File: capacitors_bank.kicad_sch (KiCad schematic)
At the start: 41 parts, among them K201 HF3F-L-12-1ZL2T, K202 HF3F-L-12-1ZL2T, K203 HF3F-L-12-1ZL2T, K204 HF3F-L-12-1ZL2T, K205 HF3F-L-12-1ZL2T, K206 HF3F-L-12-1ZL2T, K207 HF3F-L-12-1ZL2T, K208 HF3F-L-12-1ZL2T, Q201 PMOS, Q202 NMOS, Q203 PMOS, Q204 NMOS

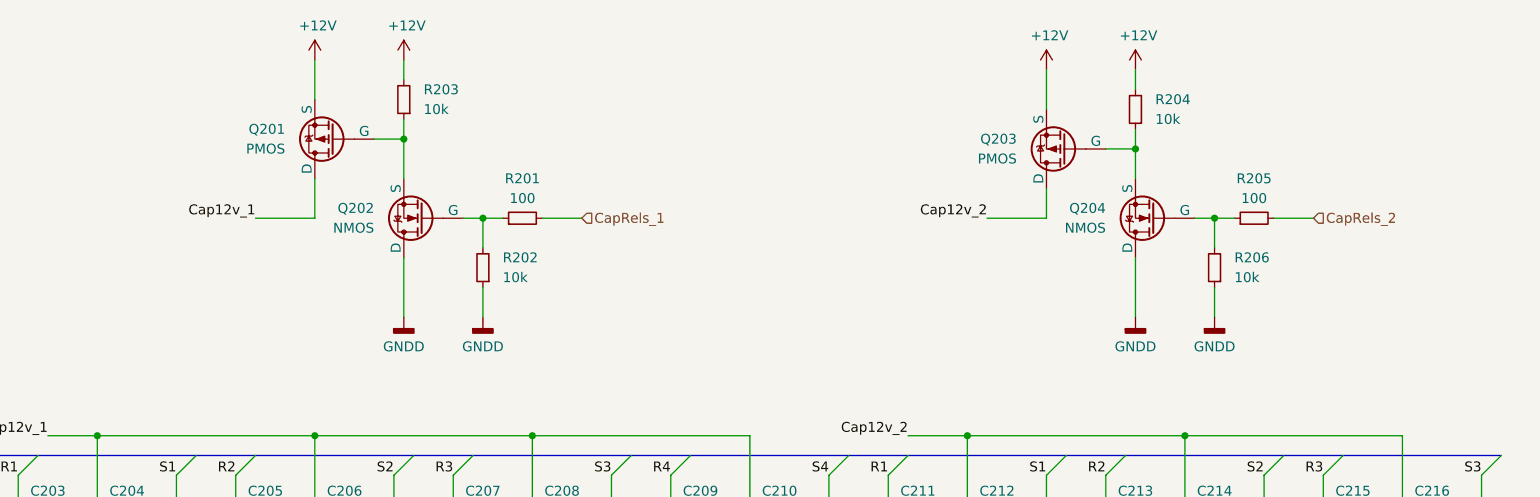
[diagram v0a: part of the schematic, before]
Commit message: Set footprints for inductors. Improved schematic of capcitors and inductors banks.
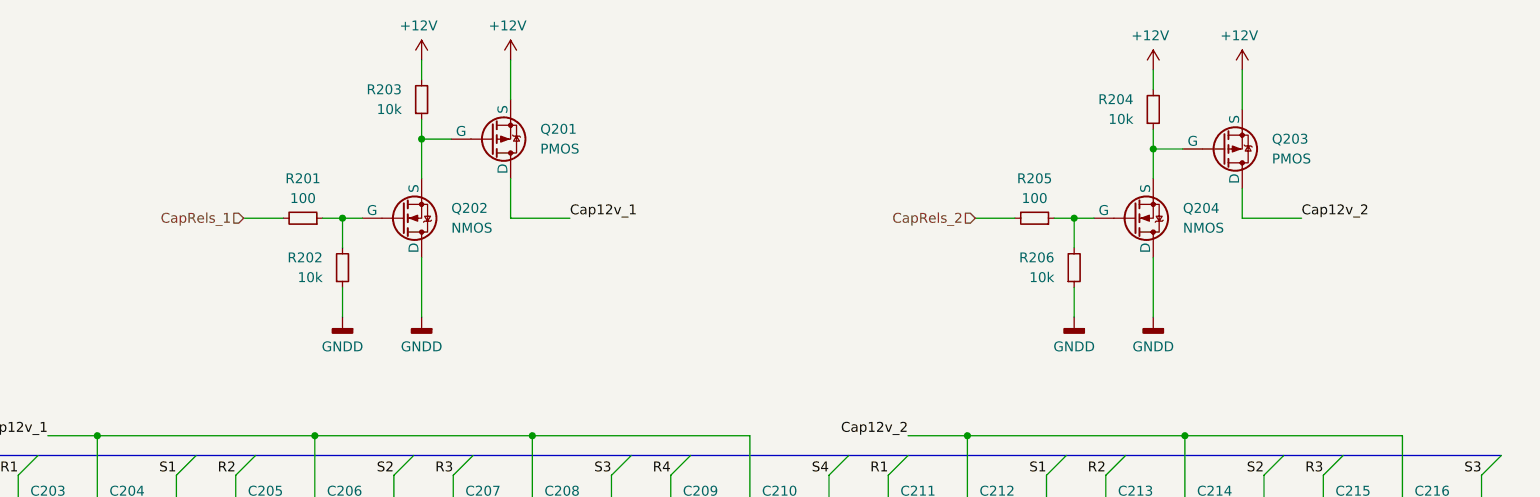
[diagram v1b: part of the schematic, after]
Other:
- moved on the sheet: Q201, Q202, Q203, Q204, R201, R202, R203, R204, R205, R206

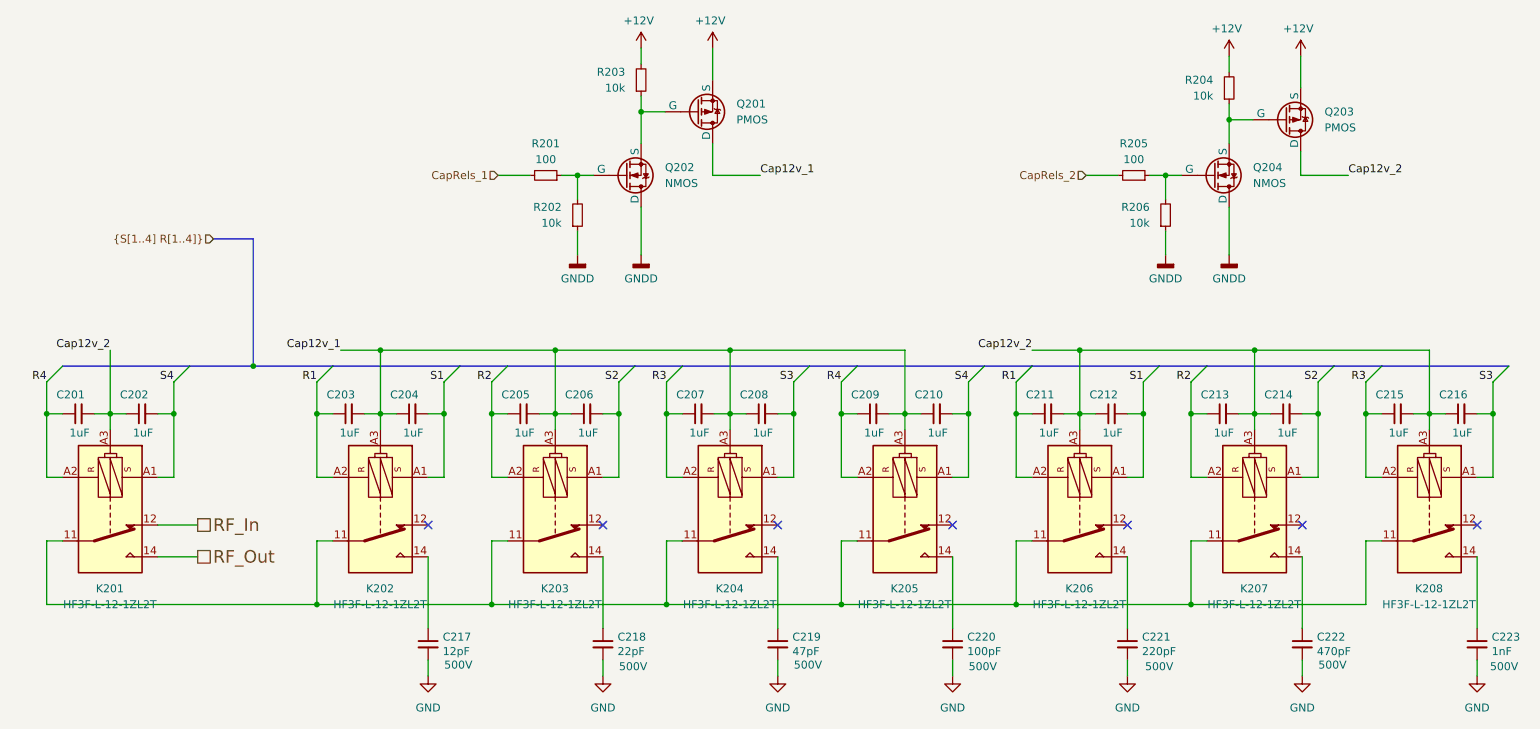
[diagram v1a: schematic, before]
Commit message: Created PDF of schematic
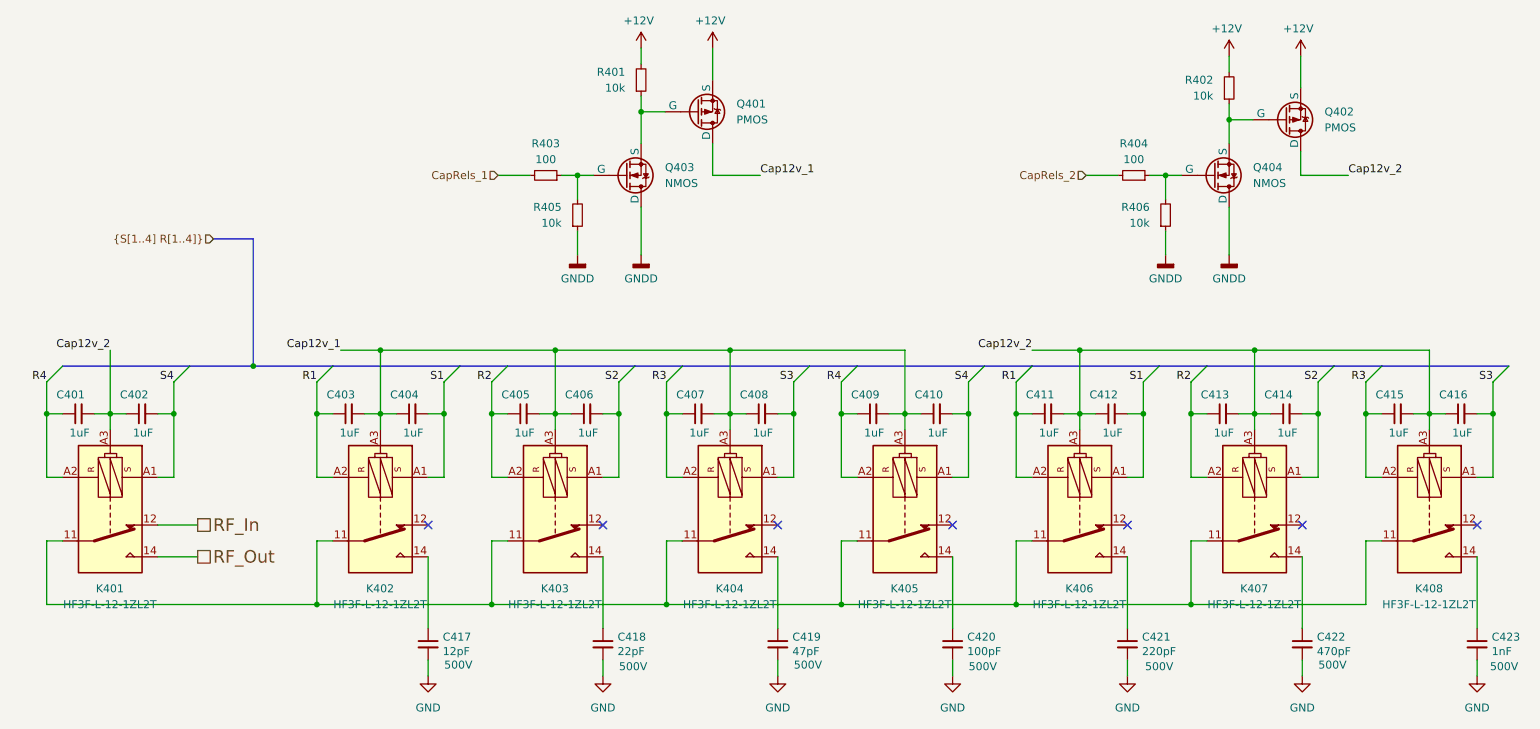
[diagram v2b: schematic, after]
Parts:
- renumbered C201 to C401, C202 to C402, C203 to C403, C204 to C404, C205 to C405, C206 to C406, C207 to C407, C208 to C408, C209 to C409, C210 to C410, C211 to C411, C212 to C412, C213 to C413, C214 to C414, C215 to C415, C216 to C416, C217 to C417, C218 to C418, C219 to C419, C220 to C420, C221 to C421, C222 to C422, C223 to C423, K201 to K401, K202 to K402, K203 to K403, K204 to K404, K205 to K405, K206 to K406, K207 to K407, K208 to K408, Q201 to Q401, Q203 to Q402, Q202 to Q403, Q204 to Q404, R203 to R401, R204 to R402, R201 to R403, R205 to R404, R202 to R405, R206 to R406

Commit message: Schematic fixes for PCB layout
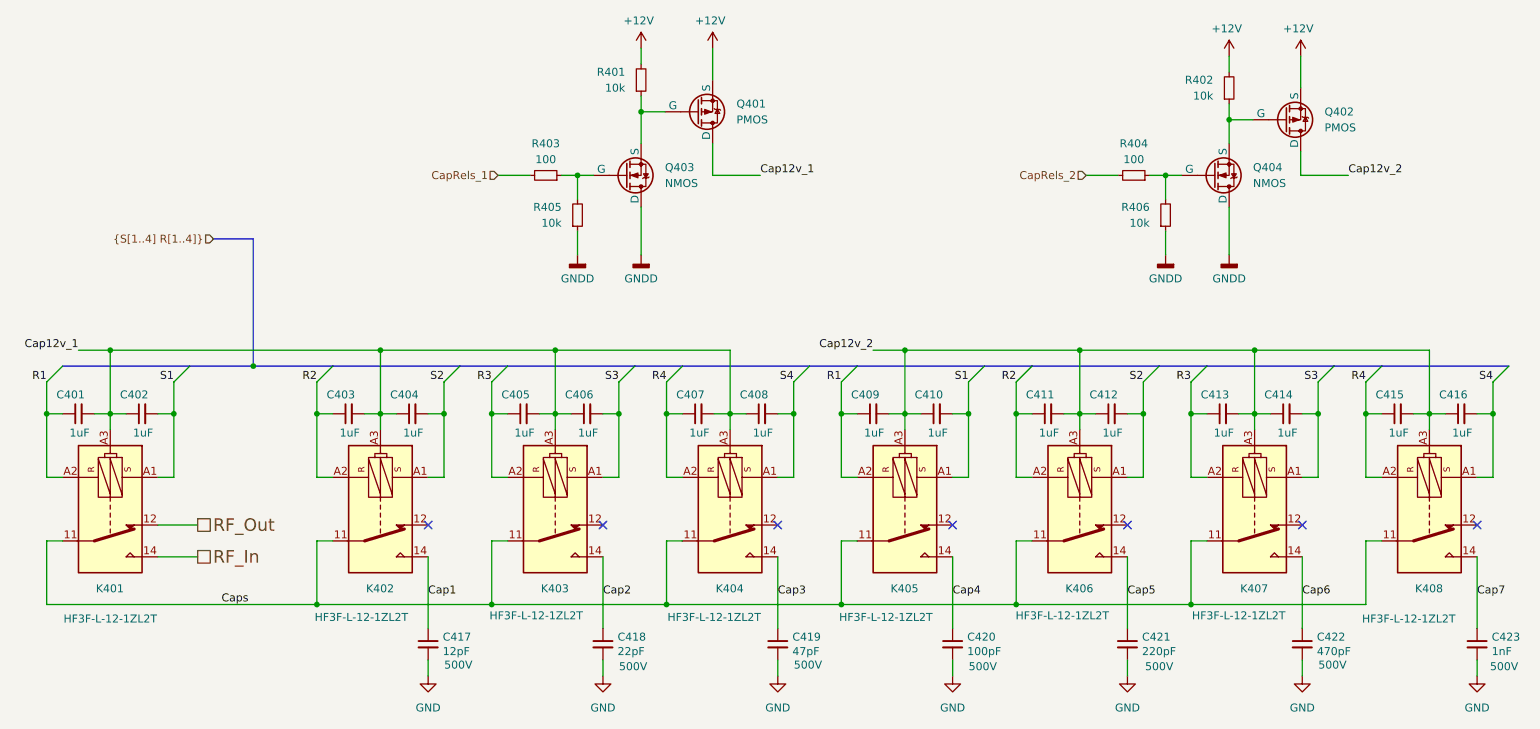
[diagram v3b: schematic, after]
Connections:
- net Cap12v_1: now also C401.2, C402.1, K401.A3; no longer C409.2, C410.1, K405.A3
- net Cap12v_2: now also C409.2, C410.1, K405.A3; no longer C401.2, C402.1, K401.A3
- net R1: now also C401.1, C409.1, K401.A2, K405.A2; no longer C403.1, C411.1, K402.A2, K406.A2
- net R2: now also C403.1, C411.1, K402.A2, K406.A2; no longer C405.1, C413.1, K403.A2, K407.A2
- net R3: now also C405.1, C413.1, K403.A2, K407.A2; no longer C407.1, C415.1, K404.A2, K408.A2
- net R4: now also C407.1, C415.1, K404.A2, K408.A2; no longer C401.1, C409.1, K401.A2, K405.A2
- net RF_In: now also K401.14; no longer K401.12
- net RF_Out: now also K401.12; no longer K401.14
- net S1: now also C402.2, C410.2, K401.A1, K405.A1; no longer C404.2, C412.2, K402.A1, K406.A1
- net S2: now also C404.2, C412.2, K402.A1, K406.A1; no longer C406.2, C414.2, K403.A1, K407.A1
- net S3: now also C406.2, C414.2, K403.A1, K407.A1; no longer C408.2, C416.2, K404.A1, K408.A1
- net S4: now also C408.2, C416.2, K404.A1, K408.A1; no longer C402.2, C410.2, K401.A1, K405.A1
- net Cap1: now reaches C417.1, K402.14
- net Caps: now reaches K401.11, K402.11, K403.11, K404.11, K405.11, K406.11, K407.11, K408.11
- net Cap2: now reaches C418.1, K403.14
- net Cap5: now reaches C421.1, K406.14
- net Cap4: now reaches C420.1, K405.14
- net Cap3: now reaches C419.1, K404.14
- net Cap6: now reaches C422.1, K407.14
- net Cap7: now reaches C423.1, K408.14
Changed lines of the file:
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@@
 	)
 	(junction
-		(at 144.78 104.14)
+		(at 127 114.3)
 		(diameter 0)
 		(color 0 0 0 0)
 	)
 	(junction
-		(at 127 114.3)
+		(at 218.44 144.78)
 		(diameter 0)
 		(color 0 0 0 0)
 	)
 	(junction
-		(at 218.44 144.78)
+		(at 172.72 114.3)
 		(diameter 0)
 		(color 0 0 0 0)
 	)
 	(junction
-		(at 172.72 114.3)
+		(at 172.72 104.14)
 		(diameter 0)
 		(color 0 0 0 0)
@@
 	)
 	(junction
+		(at 45.72 104.14)
+		(diameter 0)
+		(color 0 0 0 0)
+	)
+	(junction
 		(at 266.7 114.3)
 		(diameter 0)
@@
 	(wire
 		(pts
-			(xy 144.78 104.14) (xy 172.72 104.14)
-		)
-		(stroke
-			(width 0)
-			(type default)
-		)
-	)
-	(wire
-		(pts
 			(xy 96.52 114.3) (xy 99.06 114.3)
 		)
@@
 	(wire
 		(pts
-			(xy 82.55 104.14) (xy 88.9 104.14)
-		)
-		(stroke
-			(width 0)
-			(type default)
-		)
-	)
-	(wire
-		(pts
 			(xy 246.38 124.46) (xy 248.92 124.46)
 		)
@@
 	(wire
 		(pts
-			(xy 193.04 104.14) (xy 200.66 104.14)
-		)
-		(stroke
-			(width 0)
-			(type default)
-		)
-	)
-	(wire
-		(pts
 			(xy 127 109.22) (xy 127 114.3)
 		)
@@
 	(wire
 		(pts
+			(xy 167.64 104.14) (xy 172.72 104.14)
+		)
+		(stroke
+			(width 0)
+			(type default)
+		)
+	)
+	(wire
+		(pts
 			(xy 190.5 134.62) (xy 193.04 134.62)
 		)
@@
 	(wire
 		(pts
+			(xy 45.72 104.14) (xy 88.9 104.14)
+		)
+		(stroke
+			(width 0)
+			(type default)
+		)
+	)
+	(wire
+		(pts
 			(xy 96.52 153.67) (xy 96.52 156.21)
 		)
@@
 	(wire
 		(pts
+			(xy 40.64 104.14) (xy 45.72 104.14)
+		)
+		(stroke
+			(width 0)
+			(type default)
+		)
+	)
+	(wire
+		(pts
 			(xy 144.78 104.14) (xy 144.78 114.3)
 		)
@@
 	(wire
 		(pts
+			(xy 172.72 104.14) (xy 200.66 104.14)
+		)
+		(stroke
+			(width 0)
+			(type default)
+		)
+	)
+	(wire
+		(pts
 			(xy 224.536 81.28) (xy 224.536 88.9)
 		)
@@
 		)
 	)
+	(label "Caps"
+		(at 63.5 144.78 0)
+		(fields_autoplaced yes)
+		(effects
+			(font
+				(size 1.27 1.27)
+			)
+			(justify left bottom)
+		)
+	)
 	(label "S3"
-		(at 154.94 109.22 180)
+		(at 127 109.22 180)
 		(fields_autoplaced yes)
 		(effects
@@
 	)
 	(label "R2"
-		(at 106.68 109.22 180)
+		(at 78.74 109.22 180)
 		(fields_autoplaced yes)
 		(effects
@@
 		)
 	)
-	(label "S3"
-		(at 266.7 109.22 180)
+	(label "Cap3"
+		(at 152.4 143.51 0)
 		(fields_autoplaced yes)
 		(effects
@@
 				(size 1.27 1.27)
 			)
-			(justify right bottom)
+			(justify left bottom)
 		)
 	)
-	(label "S2"
+	(label "Cap1"
+		(at 96.52 143.51 0)
+		(fields_autoplaced yes)
+		(effects
+			(font
+				(size 1.27 1.27)
+			)
+			(justify left bottom)
+		)
+	)
+	(label "S3"
 		(at 238.76 109.22 180)
 		(fields_autoplaced yes)
@@
 		)
 	)
-	(label "S1"
+	(label "S2"
 		(at 210.82 109.22 180)
 		(fields_autoplaced yes)
@@
 		)
 	)
-	(label "S4"
+	(label "S1"
 		(at 182.88 109.22 180)
 		(fields_autoplaced yes)
@@
 		)
 	)
-	(label "S1"
-		(at 99.06 109.22 180)
+	(label "S4"
+		(at 266.7 109.22 180)
 		(fields_autoplaced yes)
 		(effects
@@
 		)
 	)
-	(label "Cap12v_2"
-		(at 193.04 104.14 180)
+	(label "S1"
+		(at 55.88 109.22 180)
 		(fields_autoplaced yes)
 		(effects
@@
 	)
 	(label "Cap12v_2"
-		(at 45.72 104.14 180)
+		(at 167.64 104.14 180)
 		(fields_autoplaced yes)
 		(effects
@@
 		)
 	)
+	(label "Cap6"
+		(at 236.22 143.51 0)
+		(fields_autoplaced yes)
+		(effects
+			(font
+				(size 1.27 1.27)
+			)
+			(justify left bottom)
+		)
+	)
+	(label "Cap4"
+		(at 180.34 143.51 0)
+		(fields_autoplaced yes)
+		(effects
+			(font
+				(size 1.27 1.27)
+			)
+			(justify left bottom)
+		)
+	)
 	(label "Cap12v_2"
 		(at 243.586 76.2 0)
@@
 	)
 	(label "Cap12v_1"
-		(at 82.55 104.14 180)
+		(at 40.64 104.14 180)
 		(fields_autoplaced yes)
 		(effects
@@
 	)
 	(label "R4"
-		(at 35.56 109.22 180)
+		(at 134.62 109.22 180)
 		(fields_autoplaced yes)
 		(effects
@@
 	)
 	(label "S2"
-		(at 127 109.22 180)
+		(at 99.06 109.22 180)
 		(fields_autoplaced yes)
 		(effects
@@
 	)
 	(label "R1"
-		(at 190.5 109.22 180)
+		(at 162.56 109.22 180)
 		(fields_autoplaced yes)
 		(effects
@@
 	)
 	(label "R3"
-		(at 134.62 109.22 180)
+		(at 106.68 109.22 180)
 		(fields_autoplaced yes)
 		(effects
@@
 		)
 	)
+	(label "Cap7"
+		(at 264.16 143.51 0)
+		(fields_autoplaced yes)
+		(effects
+			(font
+				(size 1.27 1.27)
+			)
+			(justify left bottom)
+		)
+	)
 	(label "R3"
-		(at 246.38 109.22 180)
+		(at 218.44 109.22 180)
 		(fields_autoplaced yes)
 		(effects
@@
 	)
 	(label "R4"
-		(at 162.56 109.22 180)
+		(at 246.38 109.22 180)
 		(fields_autoplaced yes)
 		(effects
@@
 	)
 	(label "S4"
-		(at 55.88 109.22 180)
+		(at 154.94 109.22 180)
 		(fields_autoplaced yes)
 		(effects
@@
 	)
 	(label "R1"
-		(at 78.74 109.22 180)
+		(at 35.56 109.22 180)
 		(fields_autoplaced yes)
 		(effects
@@
 		)
 	)
+	(label "Cap2"
+		(at 124.46 143.51 0)
+		(fields_autoplaced yes)
+		(effects
+			(font
+				(size 1.27 1.27)
+			)
+			(justify left bottom)
+		)
+	)
+	(label "Cap5"
+		(at 208.28 143.51 0)
+		(fields_autoplaced yes)
+		(effects
+			(font
+				(size 1.27 1.27)
+			)
+			(justify left bottom)
+		)
+	)
 	(label "R2"
-		(at 218.44 109.22 180)
+		(at 190.5 109.22 180)
 		(fields_autoplaced yes)
 		(effects
@@
 	(hierarchical_label "RF_Out"
 		(shape passive)
-		(at 59.69 137.16 0)
+		(at 59.69 132.08 0)
 		(fields_autoplaced yes)
 		(effects
@@
 	(hierarchical_label "RF_In"
 		(shape passive)
-		(at 59.69 132.08 0)
+		(at 59.69 137.16 0)
 		(fields_autoplaced yes)
 		(effects
@@
 		(on_board yes)
 		(dnp no)
-		(fields_autoplaced yes)
 		(property "Reference" "K403"
 			(at 116.7765 142.24 90)
@@
 		)
 		(property "Value" "HF3F-L-12-1ZL2T"
-			(at 116.7765 144.78 90)
+			(at 113.792 146.558 90)
 			(effects
 				(font
@@
 		(on_board yes)
 		(dnp no)
-		(fields_autoplaced yes)
 		(property "Reference" "K402"
 			(at 88.8365 142.24 90)
@@
 		)
 		(property "Value" "HF3F-L-12-1ZL2T"
-			(at 88.8365 144.78 90)
+			(at 85.852 146.812 90)
 			(effects
 				(font
@@
 		(on_board yes)
 		(dnp no)
-		(fields_autoplaced yes)
 		(property "Reference" "K405"
 			(at 172.6565 142.24 90)
@@
 		)
 		(property "Value" "HF3F-L-12-1ZL2T"
-			(at 172.6565 144.78 90)
+			(at 169.672 146.812 90)
 			(effects
 				(font
@@
 		(on_board yes)
 		(dnp no)
-		(fields_autoplaced yes)
 		(property "Reference" "K404"
 			(at 144.7165 142.24 90)
@@
 		)
 		(property "Value" "HF3F-L-12-1ZL2T"
-			(at 144.7165 144.78 90)
+			(at 142.24 146.812 90)
 			(effects
 				(font
@@
 		(on_board yes)
 		(dnp no)
-		(fields_autoplaced yes)
 		(property "Reference" "K406"
 			(at 200.5965 142.24 90)
@@
 		)
 		(property "Value" "HF3F-L-12-1ZL2T"
-			(at 200.5965 144.78 90)
+			(at 197.866 146.558 90)
 			(effects
 				(font
@@
 		(on_board yes)
 		(dnp no)
-		(fields_autoplaced yes)
 		(property "Reference" "K407"
 			(at 228.5365 142.24 90)
@@
 		)
 		(property "Value" "HF3F-L-12-1ZL2T"
-			(at 228.5365 144.78 90)
+			(at 226.06 146.558 90)
 			(effects
 				(font
@@
 		(on_board yes)
 		(dnp no)
-		(fields_autoplaced yes)
 		(property "Reference" "K401"
 			(at 45.6565 142.24 90)
@@
 		)
 		(property "Value" "HF3F-L-12-1ZL2T"
-			(at 45.6565 144.78 90)
+			(at 45.72 147.066 90)
 			(effects
 				(font
@@
 		(on_board yes)
 		(dnp no)
-		(fields_autoplaced yes)
 		(property "Reference" "K408"
 			(at 256.4765 142.24 90)
@@
 		)
 		(property "Value" "HF3F-L-12-1ZL2T"
-			(at 256.4765 144.78 90)
+			(at 253.238 147.066 90)
 			(effects
 				(font
